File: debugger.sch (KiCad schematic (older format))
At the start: 1 part

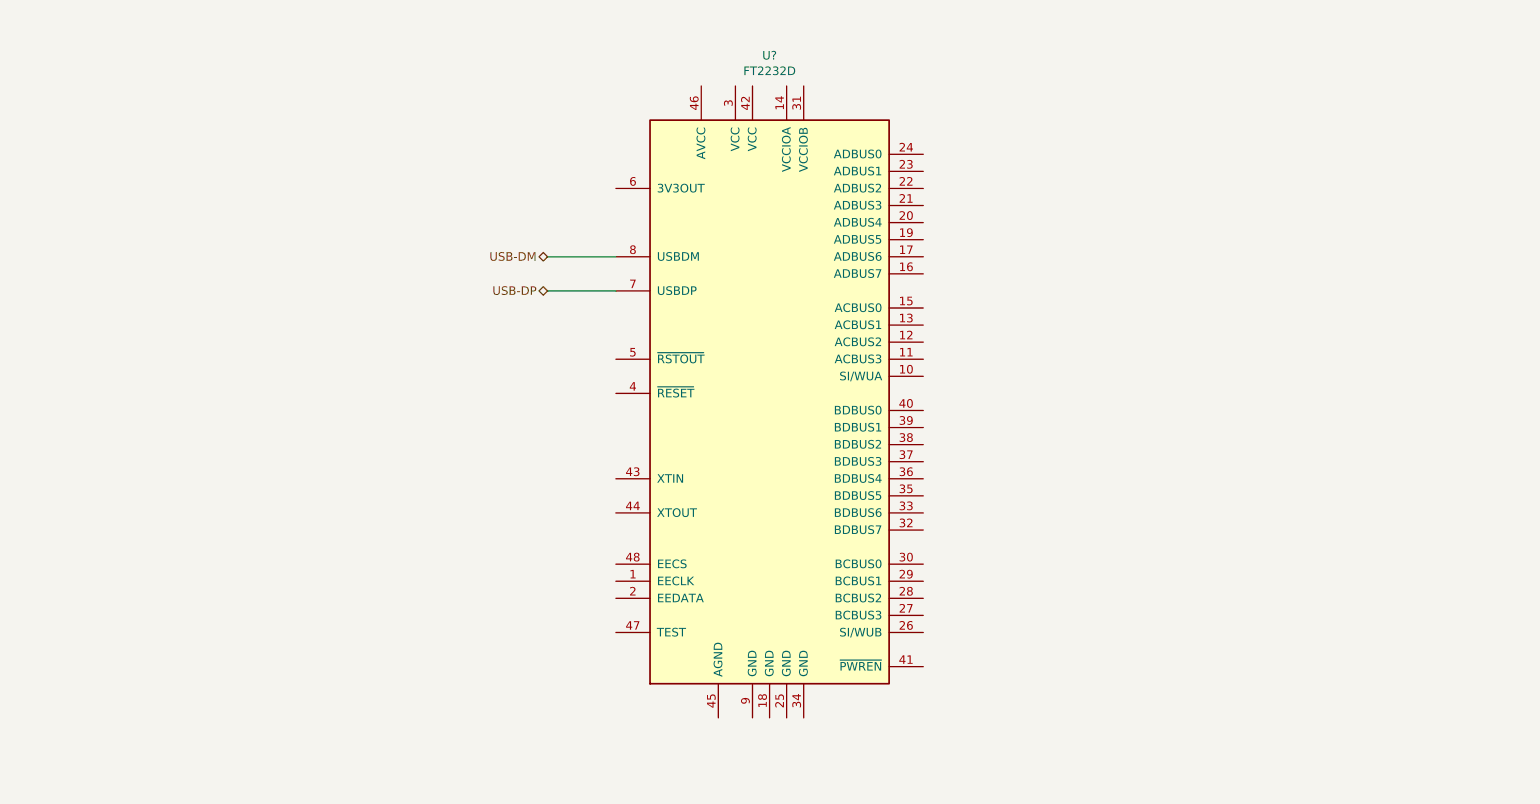
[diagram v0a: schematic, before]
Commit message: Added FT2232D and OLED connector
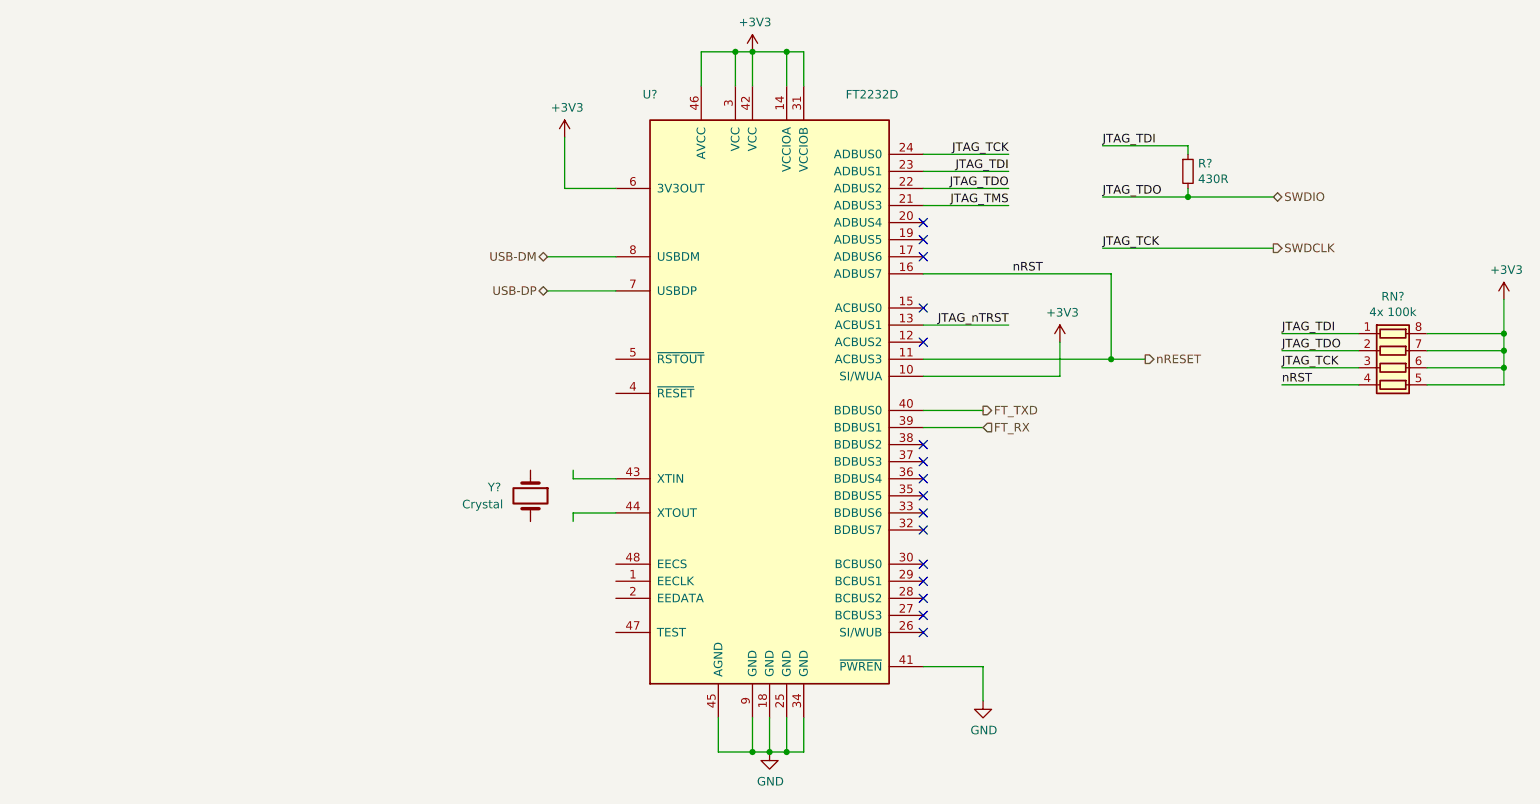
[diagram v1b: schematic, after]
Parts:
- added R?: 430R, symbol Device:R_Small
- added RN?: 4x 100k, symbol Device:R_Pack04
- added Y?: Crystal, symbol Device:Crystal
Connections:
- net labels added: +3V3, FT_RX, FT_TXD, GND, JTAG_TCK, JTAG_TDI, JTAG_TDO, JTAG_TMS, JTAG_nTRST, SWDCLK, SWDIO, nRESET, nRST
- wire segments 2 -> 59
- no-connect marks 0 -> 16

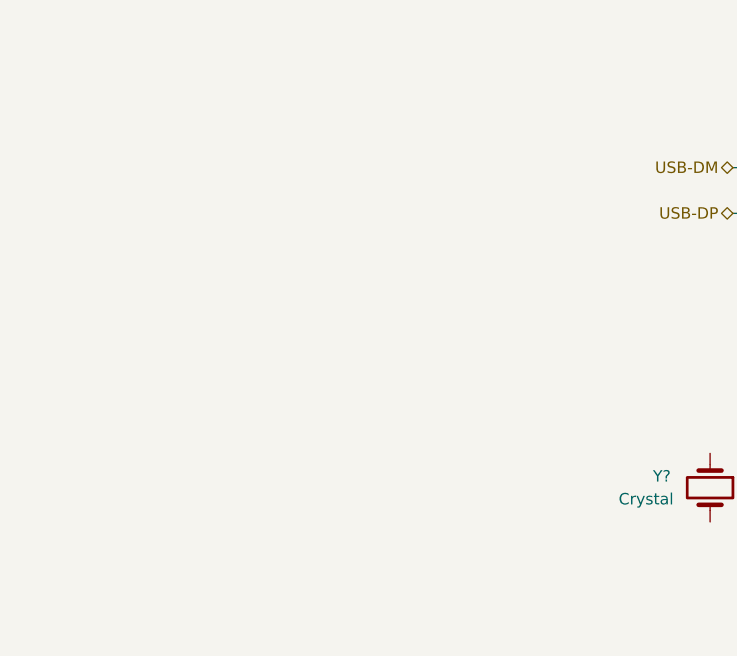
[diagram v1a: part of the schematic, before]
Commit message: Moved USB and ESD protection to debugger schematic
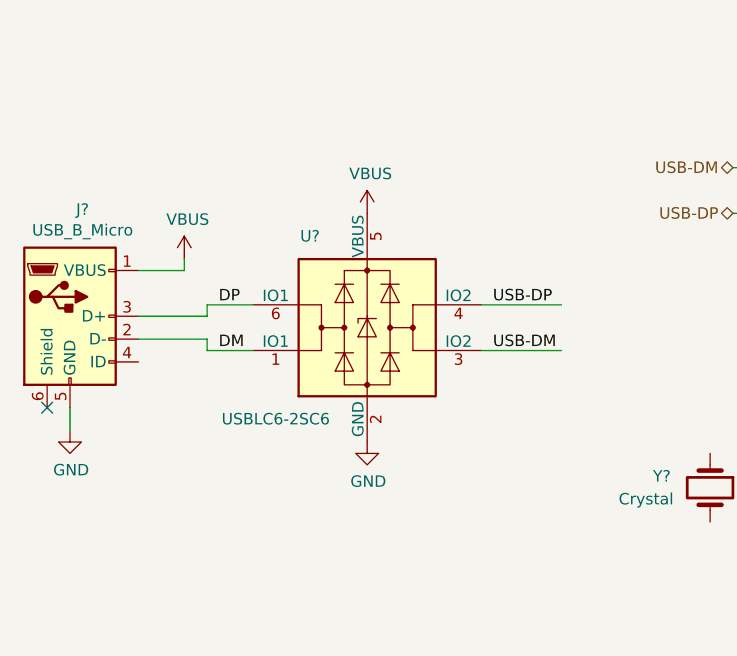
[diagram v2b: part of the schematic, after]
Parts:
- added J?: USB_B_Micro, symbol Connector:USB_B_Micro
- added U?: USBLC6-2SC6, Package_TO_SOT_SMD:SOT-23-6, symbol Power_Protection:USBLC6-2SC6
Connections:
- net labels added: DM, DP, VBUS
- wire segments 59 -> 70
- no-connect marks 16 -> 17
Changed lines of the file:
@@
 	1    0    0    -1
 $EndComp
+$Comp
+L Connector:USB_B_Micro J?
+U 1 1 5C9EA1A8
+P 1300 3650
+F 0 "J?" H 1355 4117 50  0000 C CNN
+F 1 "USB_B_Micro" H 1355 4026 50  0000 C CNN
+F 2 "" H 1450 3600 50  0001 C CNN
+F 3 "~" H 1450 3600 50  0001 C CNN
+	1    1300 3650
+	1    0    0    -1
+$EndComp
+$Comp
+L Power_Protection:USBLC6-2SC6 U?
+U 1 1 5C9EA1AF
+P 2600 3700
+F 0 "U?" H 2350 4100 50  0000 C CNN
+F 1 "USBLC6-2SC6" H 2200 3300 50  0000 C CNN
+F 2 "Package_TO_SOT_SMD:SOT-23-6" H 1850 4100 50  0001 C CNN
+F 3 "http://www2.st.com/resource/en/datasheet/CD00050750.pdf" H 2800 4050 50  0001 C CNN
+	1    2600 3700
+	1    0    0    -1
+$EndComp
+Wire Wire Line
+	1600 3450 1800 3450
+Wire Wire Line
+	1800 3450 1800 3400
+$Comp
+L power:VBUS #PWR?
+U 1 1 5C9EA1B8
+P 1800 3400
+F 0 "#PWR?" H 1800 3250 50  0001 C CNN
+F 1 "VBUS" H 1815 3573 50  0000 C CNN
+F 2 "" H 1800 3400 50  0001 C CNN
+F 3 "" H 1800 3400 50  0001 C CNN
+	1    1800 3400
+	1    0    0    -1
+$EndComp
+$Comp
+L power:VBUS #PWR?
+U 1 1 5C9EA1BE
+P 2600 3200
+F 0 "#PWR?" H 2600 3050 50  0001 C CNN
+F 1 "VBUS" H 2615 3373 50  0000 C CNN
+F 2 "" H 2600 3200 50  0001 C CNN
+F 3 "" H 2600 3200 50  0001 C CNN
+	1    2600 3200
+	1    0    0    -1
+$EndComp
+NoConn ~ 1200 4050
+Wire Wire Line
+	1300 4050 1300 4150
+$Comp
+L power:GND #PWR?
+U 1 1 5C9EA1C6
+P 1300 4150
+F 0 "#PWR?" H 1300 3900 50  0001 C CNN
+F 1 "GND" H 1305 3977 50  0000 C CNN
+F 2 "" H 1300 4150 50  0001 C CNN
+F 3 "" H 1300 4150 50  0001 C CNN
+	1    1300 4150
+	1    0    0    -1
+$EndComp
+$Comp
+L power:GND #PWR?
+U 1 1 5C9EA1CC
+P 2600 4200
+F 0 "#PWR?" H 2600 3950 50  0001 C CNN
+F 1 "GND" H 2605 4027 50  0000 C CNN
+F 2 "" H 2600 4200 50  0001 C CNN
+F 3 "" H 2600 4200 50  0001 C CNN
+	1    2600 4200
+	1    0    0    -1
+$EndComp
+Wire Wire Line
+	1600 3650 1900 3650
+Wire Wire Line
+	1900 3650 1900 3600
+Wire Wire Line
+	1900 3600 2100 3600
+Wire Wire Line
+	2100 3800 1900 3800
+Wire Wire Line
+	1900 3800 1900 3750
+Wire Wire Line
+	1900 3750 1600 3750
+Wire Wire Line
+	3100 3600 3450 3600
+Wire Wire Line
+	3100 3800 3450 3800
+Text Label 3150 3600 0    50   ~ 0
+USB-DP
+Text Label 3150 3800 0    50   ~ 0
+USB-DM
+Text Label 1950 3600 0    50   ~ 0
+DP
+Text Label 1950 3800 0    50   ~ 0
+DM
 $EndSCHEMATC
